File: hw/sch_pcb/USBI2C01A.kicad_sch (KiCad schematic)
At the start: 26 parts, among them P1 750mA, X1 CP2112, X2 USB_B, X3 SROUB3M, X4 SROUB3M, X5 SROUB3M, X6 SROUB3M

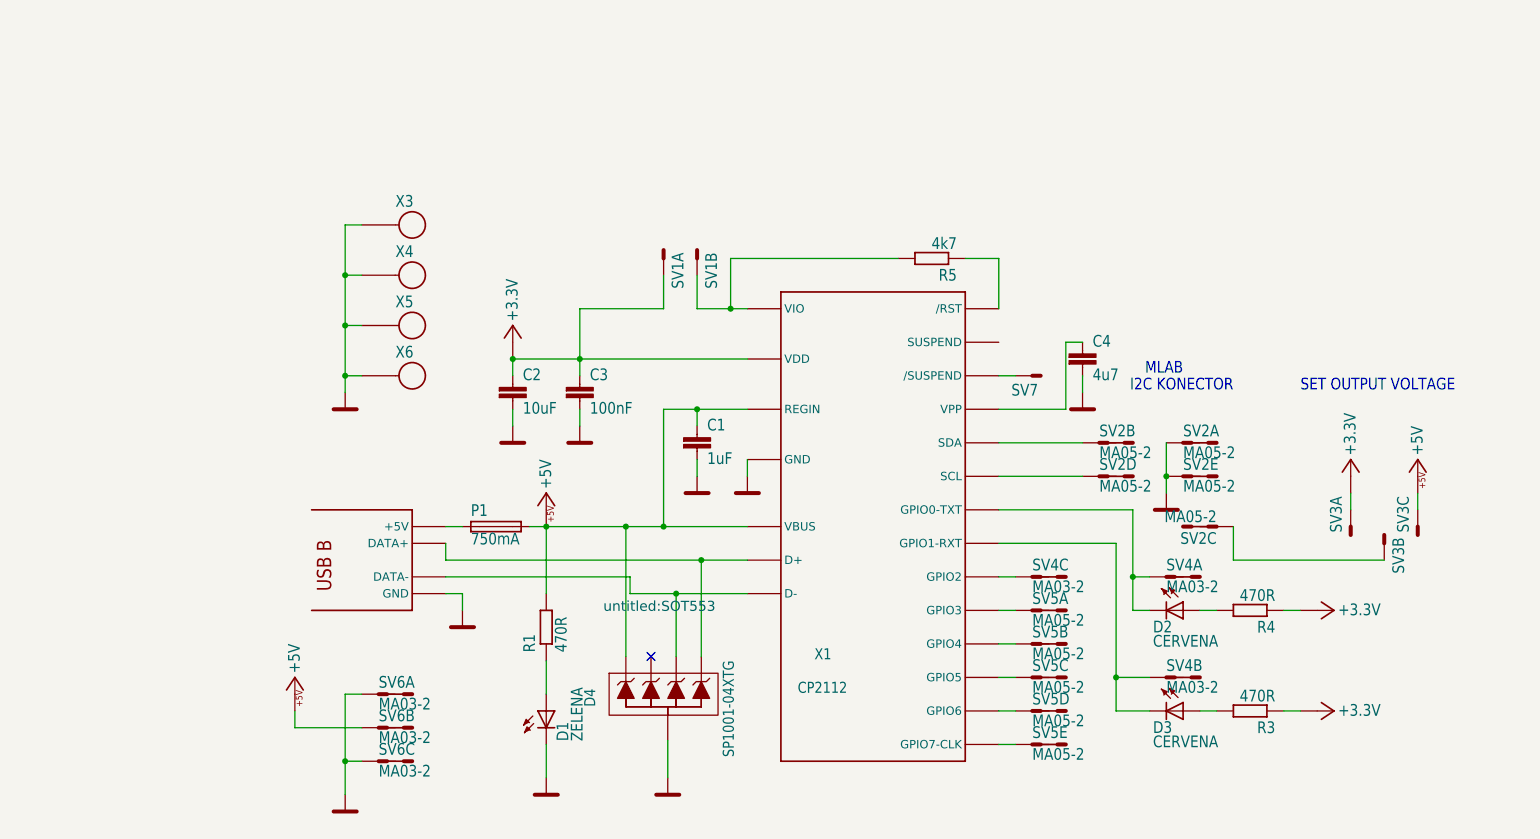
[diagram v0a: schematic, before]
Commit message: Edit schema a vlozeni UST_ID
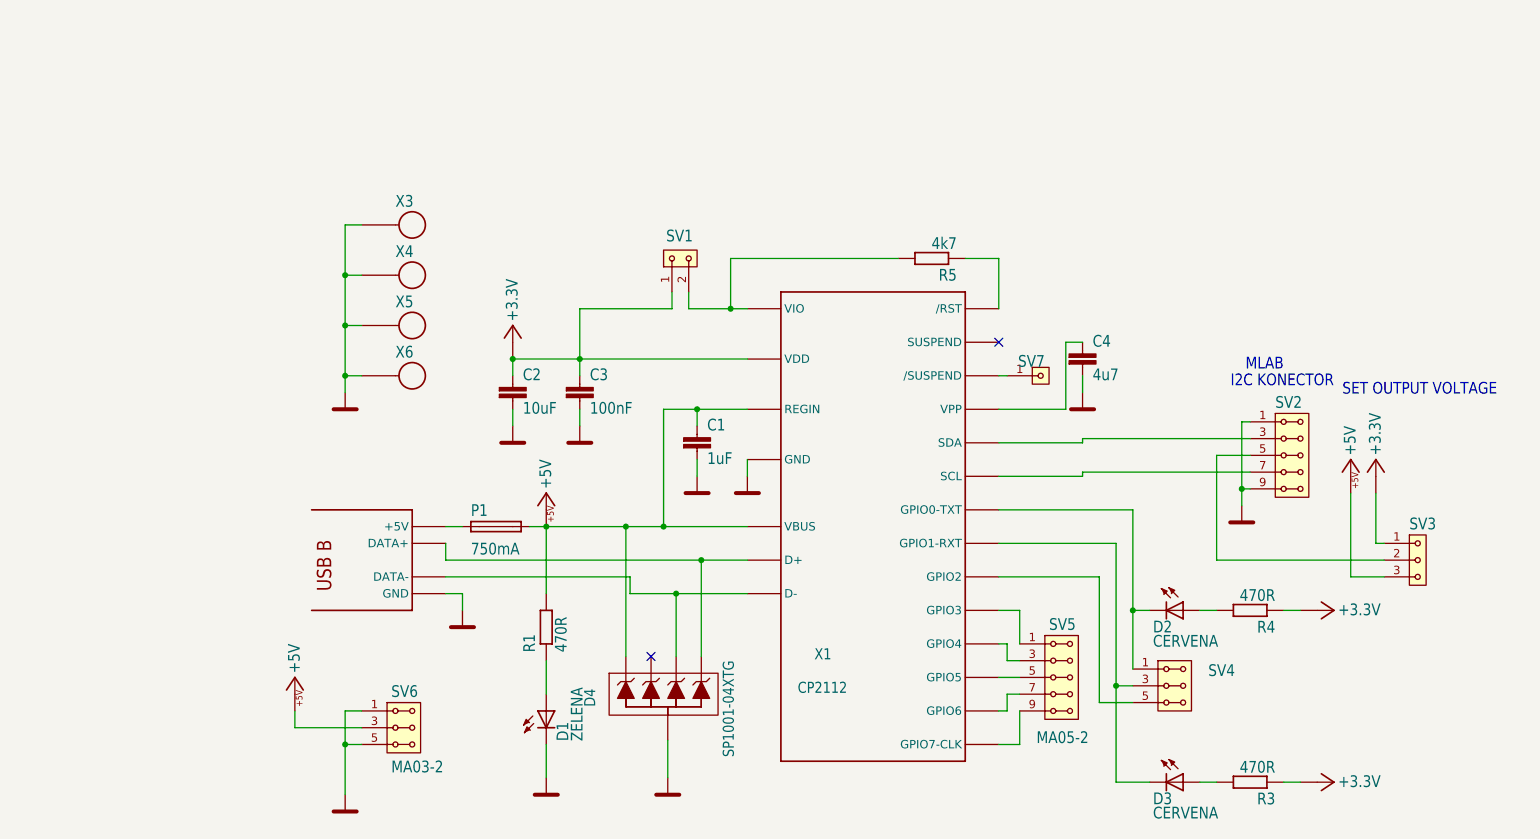
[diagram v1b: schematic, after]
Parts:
- removed unit 2 of SV1
- removed unit 4 of SV2
- removed unit 2 of SV2
- removed unit 5 of SV2
- removed unit 3 of SV2
- removed unit 2 of SV3
- removed unit 3 of SV3
- removed unit 3 of SV4
- removed unit 2 of SV4
- removed unit 4 of SV5
- removed unit 5 of SV5
- removed unit 3 of SV5
- removed unit 2 of SV5
- removed unit 3 of SV6
- removed unit 2 of SV6
- C1: UST_ID (none) -> 5c70984712875079b91f8b50
- C2: UST_ID (none) -> 5c70984812875079b91f8bbd
- C3: UST_ID (none) -> 5c70984712875079b91f8b4c
- C4: UST_ID (none) -> 5e3ff8fc1287502a33bad7a3
- D1: UST_ID (none) -> 5c70984412875079b91f8895
- D2, D3: UST_ID (none) -> 5c70984412875079b91f8896
- D4: UST_ID (none) -> 5c70984512875079b91f88cc
- P1: UST_ID (none) -> 5c70984512875079b91f88d2
- R1, R3, R4: UST_ID (none) -> 5c70984512875079b91f8986
- R5: UST_ID (none) -> 5c70984612875079b91f8995
- SV1: symbol untitled-eagle-import:MA02-1 -> MLAB_HEADER:HEADER_1x02
- SV2, SV5: symbol untitled-eagle-import:MA05-2 -> MLAB_HEADER:HEADER_2x05_PARALLEL
- SV3: symbol untitled-eagle-import:MA03-1 -> MLAB_HEADER:HEADER_1x03
- SV4, SV6: symbol untitled-eagle-import:MA03-2 -> MLAB_HEADER:HEADER_2x03_PARALLEL
- SV7: symbol untitled-eagle-import:MA01-1 -> MLAB_HEADER:HEADER_1x01
- X1: UST_ID (none) -> 5c70984612875079b91f89b2
- X2: UST_ID (none) -> 5c70984412875079b91f87a8
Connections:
- net +5V: now also SV3.3, SV6.3, SV6.4
- net GND: now also SV2.10, SV2.9, SV6.5, SV6.6
- net at R5.2, X1.P$5 (VIO): now also SV1.2
- net at X1.P$13 (GPIO6): now also SV5.7, SV5.8
- net at X1.P$12 (GPIO7-CLK): now also SV5.10, SV5.9
- net at X1.P$21 (GPIO2): now also SV4.5, SV4.6
- net at X1.P$14 (GPIO5): now also SV5.5, SV5.6
- net at X1.P$24 (SCL): now also SV2.7, SV2.8
- net at X1.P$15 (GPIO4): now also SV5.3, SV5.4
- net at X1.P$1 (SDA): now also SV2.3, SV2.4
- net at D3.K (C), X1.P$22 (GPIO1-RXT): now also SV4.3, SV4.4
- new net: SV2.5, SV2.6, SV3.2
- no-connect marks 1 -> 2
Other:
- moved on the sheet: D3, R3

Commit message: Uprava projektovych dat
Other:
- company: (none) -> MLAB
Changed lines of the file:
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@@
 (kicad_sch (version 20211123) (generator eeschema)
   (paper "A4")
+  (title_block
+    (company "MLAB")
+  )
   (junction (at 106.68 68.58) (diameter 0) (color 0 0 0 0)
   )

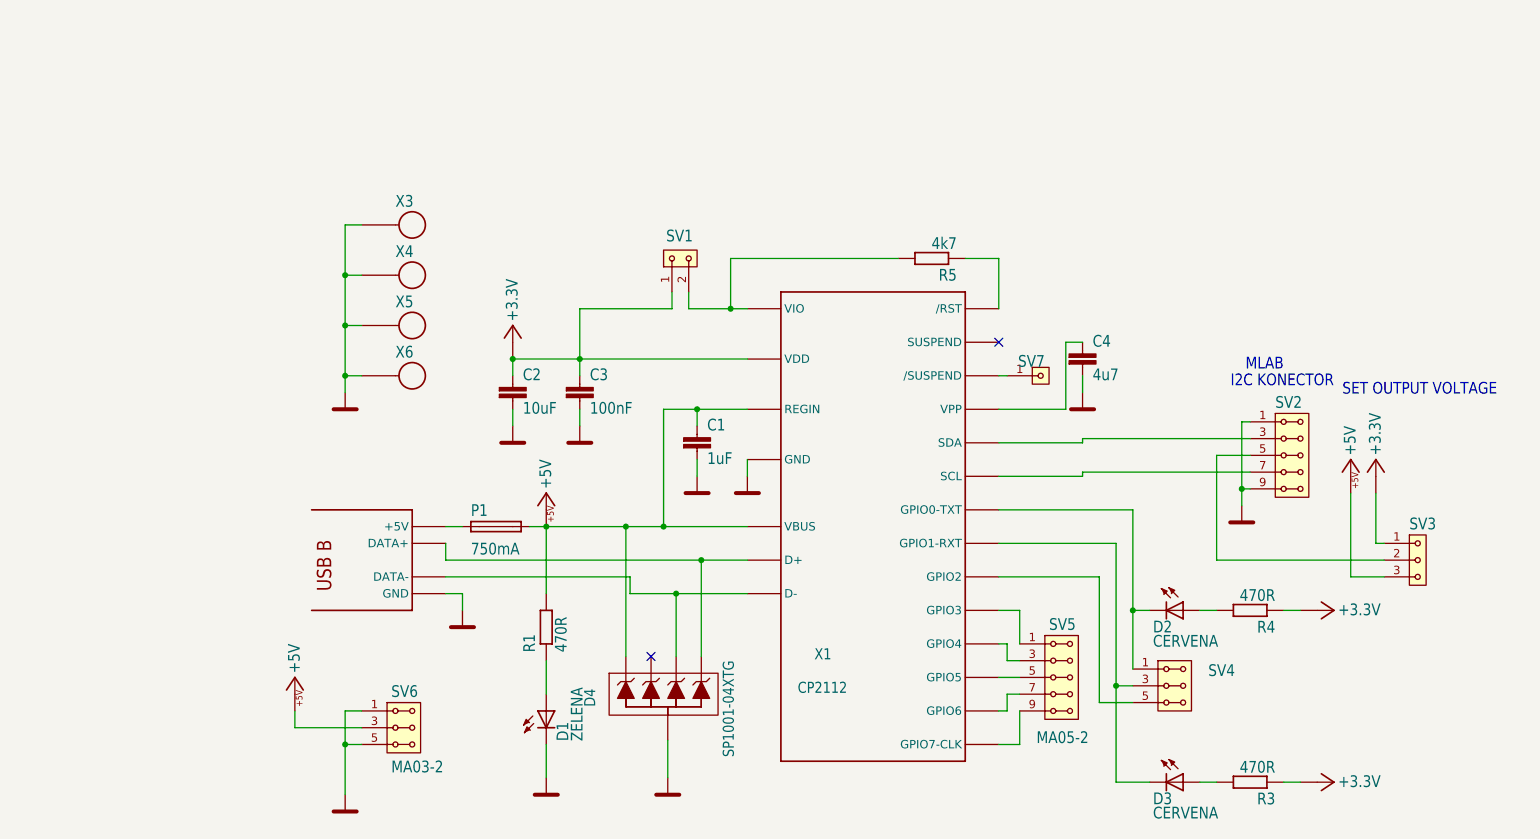
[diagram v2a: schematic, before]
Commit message: Translate and cleanup schematics.
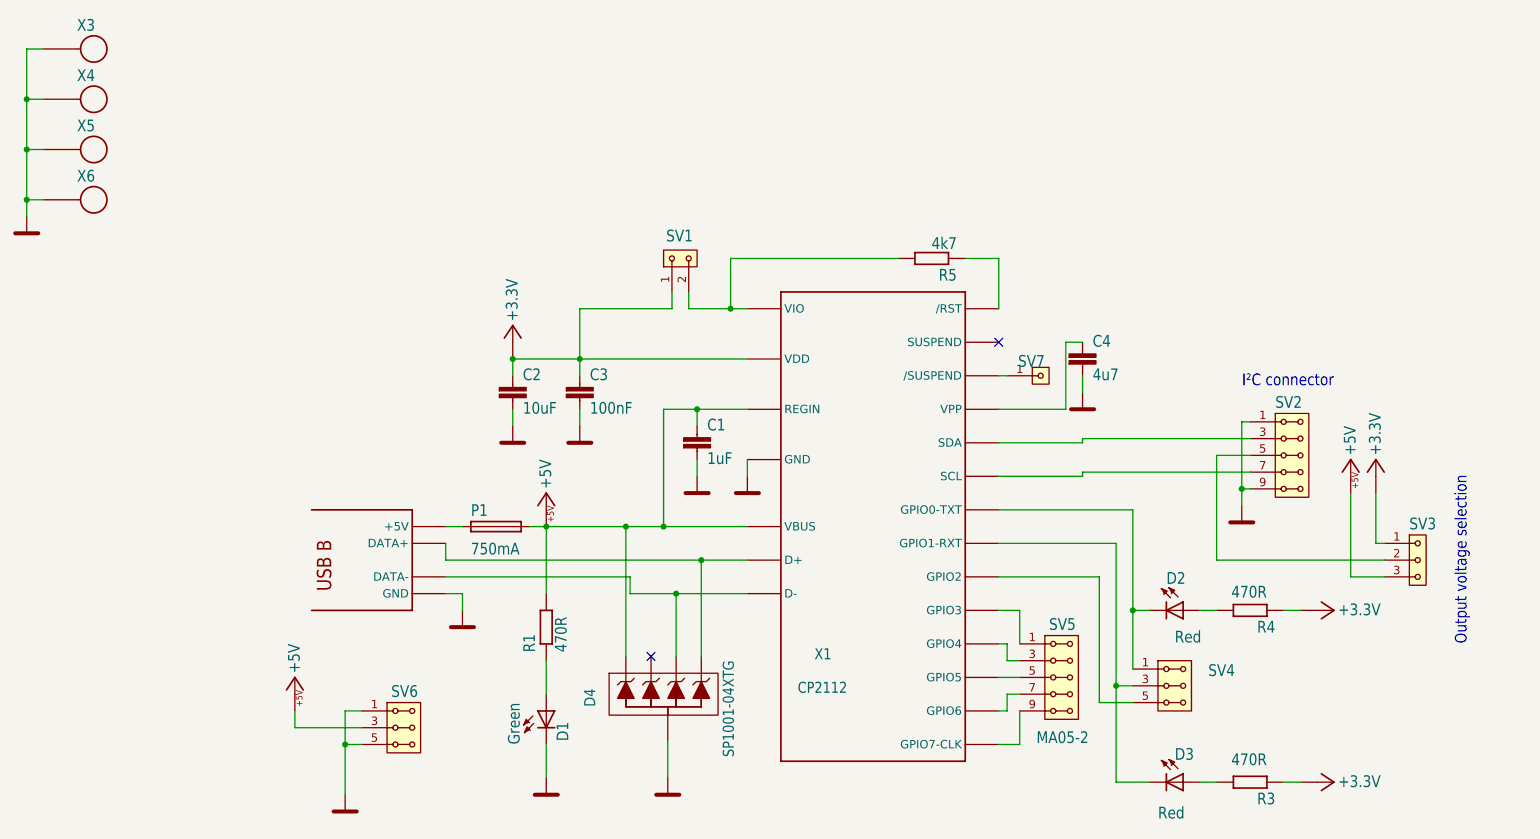
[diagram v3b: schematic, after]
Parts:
- D1: value ZELENA -> Green
- D2, D3: value CERVENA -> Red
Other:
- note added: "I²C connector"
- note added: "Output voltage selection"
- note removed: "I2C KONECTOR"
- note removed: "MLAB"
- note removed: "SET OUTPUT VOLTAGE"
- company: MLAB -> MLAB.cz
- title: (none) -> USBI2C01
- moved on the sheet: X3, X4, X5, X6
